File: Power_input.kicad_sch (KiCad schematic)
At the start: 9 parts, among them U6 AP63200WU

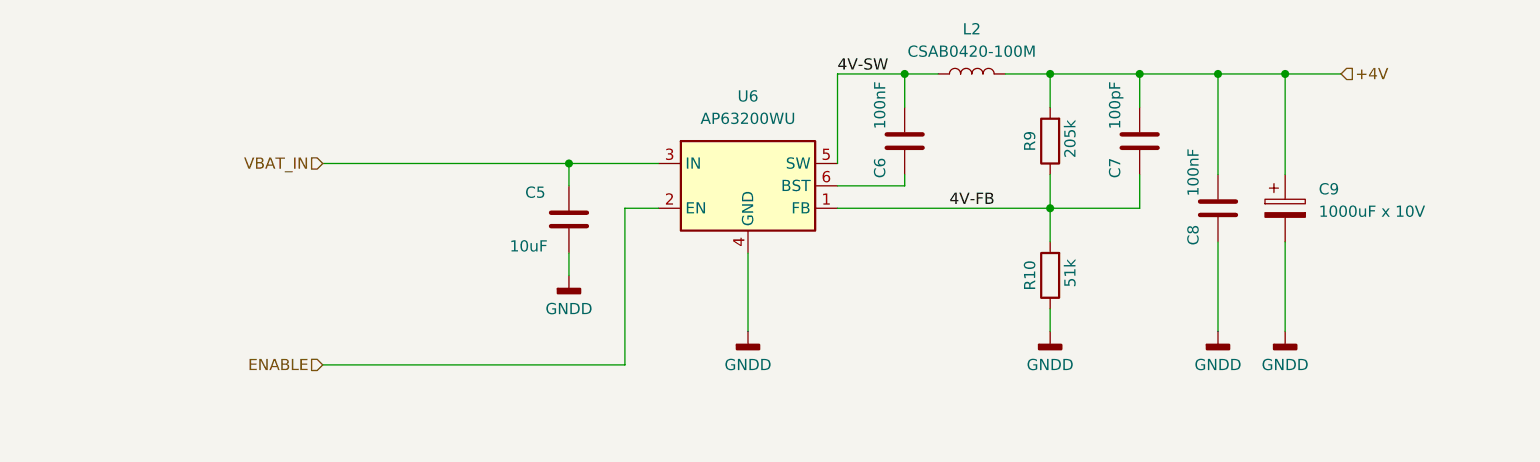
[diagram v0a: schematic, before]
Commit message: Move to SIM800C-DS and two SIM
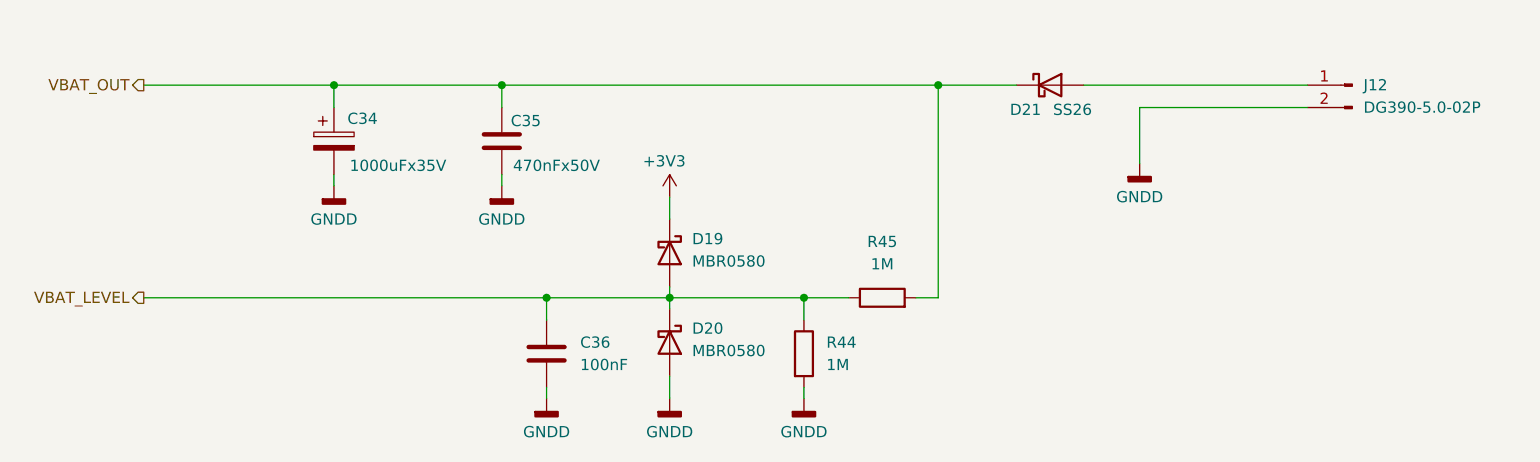
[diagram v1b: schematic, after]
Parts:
- removed C5: 10uF, Capacitor_SMD:C_0805_2012Metric_Pad1.18x1.45mm_HandSolder, symbol Device:C
- removed C6, C8: 100nF, Capacitor_SMD:C_0805_2012Metric_Pad1.18x1.45mm_HandSolder, symbol Device:C
- removed C7: 100pF, Capacitor_SMD:C_0805_2012Metric_Pad1.18x1.45mm_HandSolder, symbol Device:C
- removed C9: 1000uF x 10V, Capacitor_SMD:CP_Elec_10x10.5, symbol Device:C_Polarized
- removed L2: CSAB0420-100M, footprints:CSAB0420-4.4x4.4mm, symbol Device:L
- removed R10: 51k, Resistor_SMD:R_0805_2012Metric_Pad1.20x1.40mm_HandSolder, symbol Device:R
- removed R9: 205k, Resistor_SMD:R_0805_2012Metric_Pad1.20x1.40mm_HandSolder, symbol Device:R
- removed U6: AP63200WU, Package_TO_SOT_SMD:TSOT-23-6, symbol Regulator_Switching:AP63200WU
- added C34: 1000uFx35V, Capacitor_THT:CP_Radial_D12.5mm_P5.00mm, symbol Device:C_Polarized
- added C35: 470nFx50V, Capacitor_SMD:C_0805_2012Metric_Pad1.18x1.45mm_HandSolder, symbol Device:C
- added C36: 100nF, Capacitor_SMD:C_0805_2012Metric_Pad1.18x1.45mm_HandSolder, symbol Device:C
- added D19, D20: MBR0580, Diode_SMD:D_SOD-123, symbol Diode:MBR0580
- added D21: SS26, Diode_SMD:D_SMA, symbol Diode:SS26
- added J12: DG390-5.0-02P, footprints:DEGSON_DG390-5.0-02P_1x02_P5.0mm_Vertical, symbol symbols:Conn_DEGSON_01x02_Pin
- added R44, R45: 1M, Resistor_SMD:R_0805_2012Metric_Pad1.20x1.40mm_HandSolder, symbol Device:R
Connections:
- net GNDD: now also C34.2, C35.2, C36.1, D20.2 (A), J12.2 (Pin_2), R44.2
- new net: D21.2 (A), J12.1 (Pin_1)
- new net +3V3: D19.1 (K)
- new net VBAT_LEVEL: C36.2, D19.2 (A), D20.1 (K), R44.1, R45.1
- new net VBAT_OUT: C34.1, C35.1, D21.1 (K), R45.2

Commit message: Proproduction version
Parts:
- added D20: SMAJ30CA, Diode_SMD:D_SMA, symbol Diode:SMAJ30CA
- R44: value 1M -> 100k; MPN RC0805JR-071ML -> RC0805JR-07100KL
- renumbered C34 to C33, C35 to C34, C36 to C35, D19 to D17, D20 to D18, D21 to D19
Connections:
- net GNDD: now also D20.1 (A1)
- net Vsupply: now reaches D19.2 (A), J12.1 (Pin_1)
- net Vsupply: now also D20.2 (A2)
